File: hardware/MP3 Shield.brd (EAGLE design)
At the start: 53.3 x 59.7 mm, 52 parts, among them Q1 12.288MHz, U1 3.3V, U2 ARDUINO_SHIELD, U3 VS1053, U4 1.8V, U6 USD-SOCKET, U7 74HC4050 LVL CONVERTER

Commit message: More WIP.
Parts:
- removed U$7: LOGO-SFENEW, SparkFun:SFE-NEW-WEBLOGO
- removed U5: (no value), SparkFun:AUDIO-JACK-3.5MM-SMD
- added C17, C18: 10uF, SparkFun-Capacitors:EIA3216
- added C19, C20: 3.3nF, SparkFun-Capacitors:0603-CAP
- added J1: ISP/SPI, SparkFun:2X3
- added LOGO1: OSHW-LOGOS, SparkFun-Aesthetics:OSHW-LOGO-S
- added LOGO2: SFE_LOGO_NAME_FLAME.1_INCH, SparkFun-Aesthetics:SFE_LOGO_NAME_FLAME_.1
- added R15, R16: 10K, SparkFun-Resistors:0603-RES
- added R21, R22: 470, SparkFun-Resistors:0603-RES
- added R23: 1K, SparkFun-Resistors:0603-RES
- added SJ4: NC, SparkFun:SJ_2S-TRACE
- added SJ7, SJ8, SJ9: JUMPER-PAD-3-2OF3_NC_BY_TRACE, SparkFun-Passives:PAD-JUMPER-3-2OF3_NC_BY_TRACE_YES_SILK_FULL_BOX
- C1, C6: device SparkFun:EIA3216 -> SparkFun-Capacitors:EIA3216
- C10, C11, C12, C13, C14, C15, C16, C2, C3, C4, C5, C7, C8, C9: device SparkFun:0402-CAP -> SparkFun-Capacitors:0603-CAP
- JP1: value Line Output -> (none); device SparkFun:1X03 -> SparkFun-Connectors:AUDIO-JACK-3.5MM-SMD
- JP3: value External Speaker -> Optional
- LED1: device SparkFun:LED-0603 -> SparkFun-LED:LED-0603
- R1, R10, R11, R12, R13, R14, R2, R3, R4, R5, R6, R7, R8, R9: device SparkFun:0402-RES -> SparkFun-Resistors:0603-RES
- S2: device SparkFun:TACTILE_SWITCH_SMD -> SparkFun-Electromechanical:TACTILE_SWITCH_SMD
- U1: device SparkFun:SOT23-5 -> SparkFun-PowerIC:SOT23-5
- U2: value ARDUINO_SHIELD -> ARDUINO_R3_SHIELD; device SparkFun:DUEMILANOVE_SHIELD -> SparkFun-Boards:UNO_R3_SHIELD
- U3: device SparkFun:LQFP-48 -> SparkFun-DigitalIC:LQFP-48
- U4: device SparkFun:SC70 -> SparkFun-PowerIC:SC70
- U7: device SparkFun:SO016 -> SparkFun-DigitalIC:SO016
- moved JP1 73.8 mm to (27.9, 0.00), turned to 90 degrees
- moved C1 10.2 mm to (43.2, 35.6)
- moved LED1 10.2 mm to (43.2, 53.3), turned to 90 degrees
- moved R8 10.2 mm to (43.2, 52.1)
- moved C2 10.2 mm to (43.2, 38.1)
- moved U4 10.2 mm to (43.2, 40.6)
- moved C4 10.2 mm to (43.2, 50.8)
- moved C5 10.2 mm to (43.2, 45.7)
- moved C6 10.2 mm to (43.2, 43.2)
- moved TP1 10.2 mm to (40.6, 45.7)
- moved U1 10.2 mm to (43.2, 48.3)
- moved U$8 6.35 mm to (36.1, 46.1)
- moved S2 6.35 mm to (49.5, 12.7), turned to 90 degrees
- moved C12 1.80 mm to (38.1, 34.3)
- moved C10 1.80 mm to (38.1, 33.0)
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- renumbered SJ1 to SJ3
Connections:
- net N$1 renamed RCAP
- net N$73 renamed GPIO4
- new net /MUTE: R23.1
- new net 5V-MUTE: SJ4.2, U2.D5
- new net N$14: R23.2, SJ4.1
- new net N$17: C18.A, C20.1, R22.1
- new net N$19: C17.A, C19.1, R21.1
- new net SPKR-L: C17.C, R15.1
- new net SPKR-R: C18.C, R16.1
- net 3.3V: no longer R5.1
- net 5V-MOSI: now also J1.4
- net 5V-SCK: now also J1.3
- net GBUF: no longer JP3.1, U5.SLEEVE
- net GND: now also C19.2, C20.2, J1.6, R15.2, R16.2, R5.1, SJ9.1
- net LEFT: now also R21.2; no longer JP3.3, U5.TIP
- net MISO: now also J1.1
- net RIGHT: now also R22.2; no longer JP3.2, U5.RING
- net VCC: now also J1.2
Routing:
- net 5V-SCK: track 16.5 -> 95.7 mm
- net 5V-MUTE: track 0.00 -> 65.6 mm, vias 0 -> 4
- net 5V-MOSI: track 13.3 -> 65.5 mm
- net MISO: track 53.3 -> 102.7 mm
- net VCC: track 17.5 -> 59.1 mm
- net RIGHT: track 50.6 -> 14.5 mm
- net 3.3V: track 129.2 -> 161.7 mm, vias 6 -> 8
- net LEFT: track 50.1 -> 32.3 mm
- net ARST: track 5.34 -> 15.3 mm
- net 1.8V: track 47.6 -> 54.0 mm, vias 3 -> 4
- net SPKR-L: track 0.00 -> 6.16 mm
- net MP3-RST: track 39.9 -> 45.4 mm
- net N$19: track 0.00 -> 5.06 mm
- net N$17: track 0.00 -> 5.06 mm
- net GND: track 20.0 -> 24.4 mm, vias 14 -> 17
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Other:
- board text added: "GBUF"
- board text added: "GND"
- board text added: "MP3 Player"
- board text added: "MUTE"
- board text added: "SJ1"
- board text added: "SPI"
- board text added: "Shield"
- board text added: "v1.4"
- board text removed: "4-1-11"

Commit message: Yet more WIP
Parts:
- removed R23: 1K, SparkFun-Resistors:0603-RES
- removed SJ7, SJ8, SJ9: JUMPER-PAD-3-2OF3_NC_BY_TRACE, SparkFun-Passives:PAD-JUMPER-3-2OF3_NC_BY_TRACE_YES_SILK_FULL_BOX
- added SJ1: NC, SparkFun:SJ_2S-TRACE
- added SJ5: AC Coupling L, SparkFun-Passives:PAD-JUMPER-3-2OF3_NC_BY_TRACE_YES_SILK_FULL_BOX
- SJ3: value NC -> AC Coupling Gnd; device SparkFun:SJ_2S-TRACE -> SparkFun-Passives:PAD-JUMPER-3-2OF3_NC_BY_TRACE_YES_SILK_FULL_BOX
- SJ4: value NC -> AC Coupling R; device SparkFun:SJ_2S-TRACE -> SparkFun-Passives:PAD-JUMPER-3-2OF3_NC_BY_TRACE_YES_SILK_FULL_BOX
- moved SJ3 43.0 mm to (38.1, 8.89), turned to 90 degrees
- moved R15 16.5 mm to (41.9, 24.1), turned to 0 degrees
- moved C17 14.0 mm to (35.6, 26.7), turned to 180 degrees
- moved R16 13.1 mm to (41.9, 30.5), turned to 0 degrees
- moved SJ4 10.9 mm to (38.1, 19.1), turned to 90 degrees
- moved C19 8.89 mm to (38.1, 24.1)
- moved R21 8.89 mm to (34.3, 24.1)
- moved C18 7.18 mm to (41.9, 27.9), turned to 180 degrees
- moved C20 5.08 mm to (38.1, 30.5)
- moved R22 5.08 mm to (34.3, 30.5)
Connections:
- removed net /MUTE: R23.1
- removed net 5V-MUTE: SJ4.2, U2.D5
- new net N$12: JP1.SLEEVE, JP3.1, SJ3.2
- new net N$13: JP1.RING, JP3.2, SJ4.2
- net 5V-GPIO1: now also SJ1.2; no longer SJ3.2
- net GBUF: now also SJ3.3
- net GND: now also SJ3.1; no longer SJ9.1
- net LEFT: now also SJ5.3
- net N$14: now also JP1.TIP, JP3.3, SJ5.2; no longer R23.2, SJ4.1
- net N$4: now also SJ1.1; no longer SJ3.1
- net RIGHT: now also SJ4.3
- net SPKR-L: now also SJ5.1
- net SPKR-R: now also SJ4.1
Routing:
- net 5V-MUTE: track 65.6 -> 0.00 mm, vias 4 -> 0
- net GBUF: track 43.5 -> 9.57 mm, vias 2 -> 1
- net 3.3V: track 161.7 -> 129.0 mm, vias 8 -> 5
- net LEFT: track 32.3 -> 15.8 mm, vias 2 -> 1
- net RIGHT: track 14.5 -> 7.54 mm, vias 2 -> 1
- net SPKR-L: track 6.16 -> 0.00 mm
- net N$19: track 5.06 -> 0.00 mm
- net N$17: track 5.06 -> 0.00 mm
- net SPKR-R: track 3.60 -> 0.00 mm
- net N$14: track 2.68 -> 0.00 mm
- net /MUTE: track 1.32 -> 0.00 mm
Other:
- board text added: "SJ3"
- board text added: "SJ3, SJ4, SJ5 -> for headphone output <- for line output"
- board text added: "SJ4"
- board text added: "SJ5"
- board text removed: "GBUF"
- board text removed: "GND"
- board text removed: "SJ1"

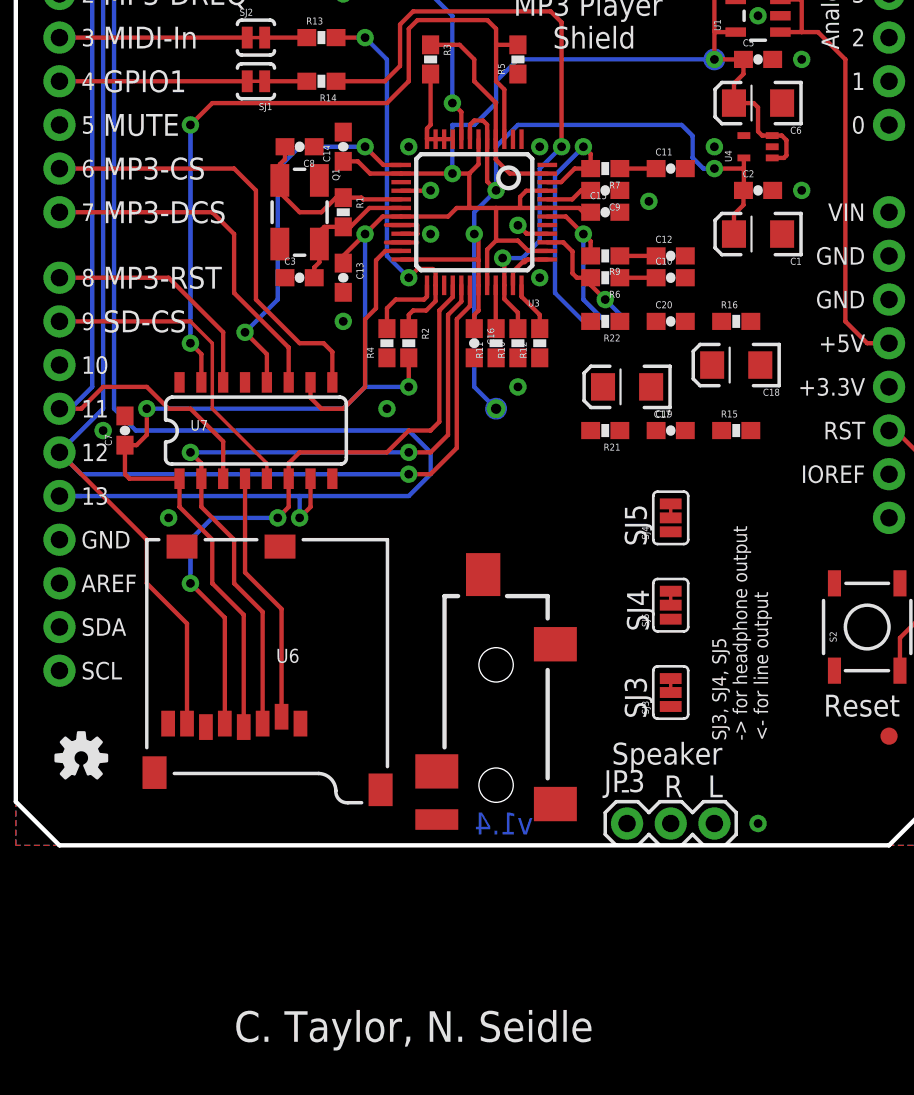
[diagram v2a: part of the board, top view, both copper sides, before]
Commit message: V1.5 ready for protos.
Board routed and ready for protos.
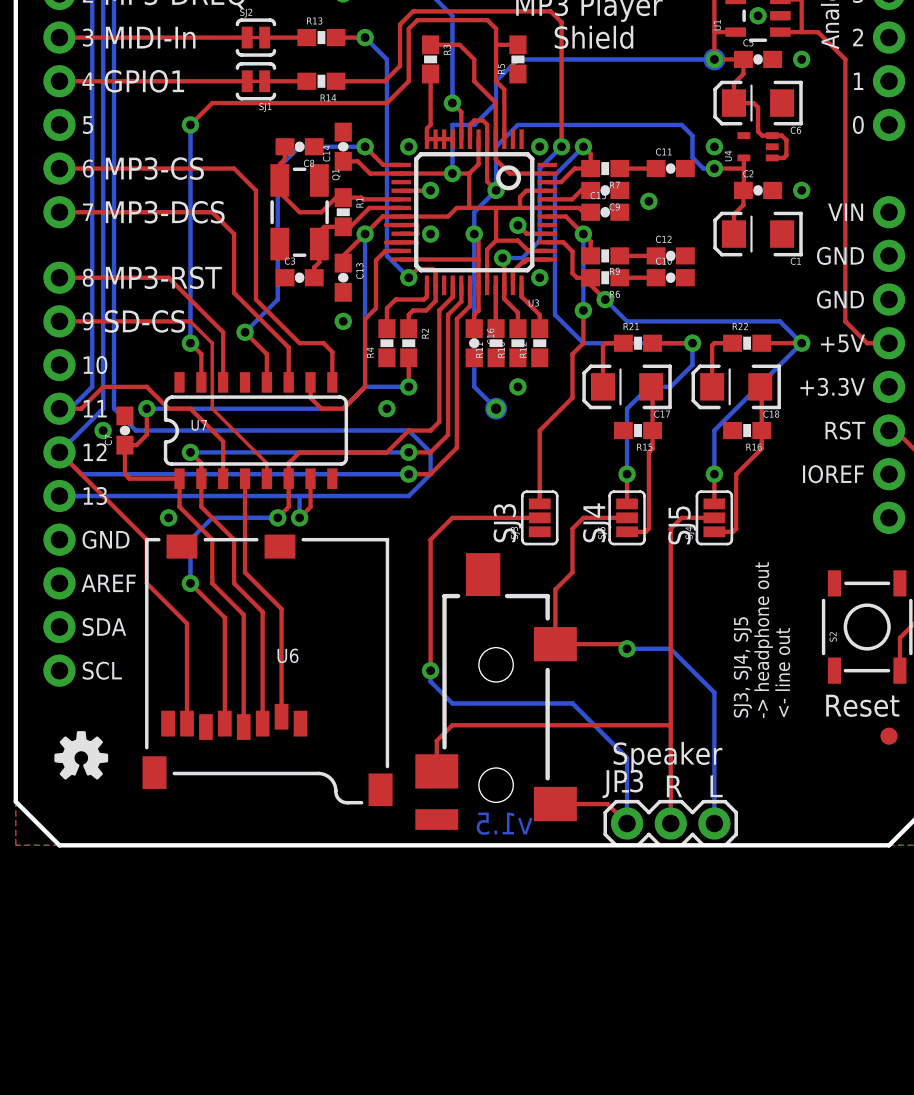
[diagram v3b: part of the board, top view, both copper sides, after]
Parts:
- removed C19, C20: 3.3nF, SparkFun-Capacitors:0603-CAP
- SJ3, SJ4, SJ5: device SparkFun-Passives:PAD-JUMPER-3-2OF3_NC_BY_TRACE_YES_SILK_FULL_BOX -> SparkFun-Passives:PAD-JUMPER-3-2OF3_NC_BY_PASTE_YES_SILK_FULL_BOX
- moved U$1 31.7 mm to (-7.62, -27.9)
- moved SJ3 12.7 mm to (30.5, 19.1)
- moved R22 8.35 mm to (42.5, 29.2), turned to 0 degrees
- moved R16 6.38 mm to (42.5, 24.1), turned to 180 degrees
- moved R15 5.71 mm to (36.2, 24.1), turned to 180 degrees
- moved SJ5 5.68 mm to (35.6, 19.1)
- moved R21 5.43 mm to (36.2, 29.2), turned to 0 degrees
- moved SJ4 2.54 mm to (40.6, 19.1)
- moved C18 1.27 mm to (41.9, 26.7)
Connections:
- net GND: no longer C19.2, C20.2
- net N$17: no longer C20.1
- net N$19: no longer C19.1
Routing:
- net N$12: track 0.00 -> 36.9 mm, vias 0 -> 1
- net N$13: track 0.00 -> 35.7 mm
- net N$14: track 0.00 -> 28.6 mm, vias 0 -> 1
- net RIGHT: track 7.54 -> 32.0 mm, vias 1 -> 3
- net LEFT: track 15.8 -> 37.4 mm, vias 1 -> 3
- net GBUF: track 9.57 -> 20.7 mm, vias 1 -> 2
- net SPKR-R: track 0.00 -> 10.2 mm
- net SPKR-L: track 0.00 -> 9.72 mm
- net N$19: track 0.00 -> 3.65 mm
- net N$17: track 0.00 -> 3.65 mm
- net GND: vias 17 -> 16
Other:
- board text added: "Byron Jacquot"
- board text added: "SJ3, SJ4, SJ5 -> headphone out <- line out"
- board text added: "v1.5"
- board text removed: "MUTE"
- board text removed: "SJ3, SJ4, SJ5 -> for headphone output <- for line output"
- board text removed: "v1.4"

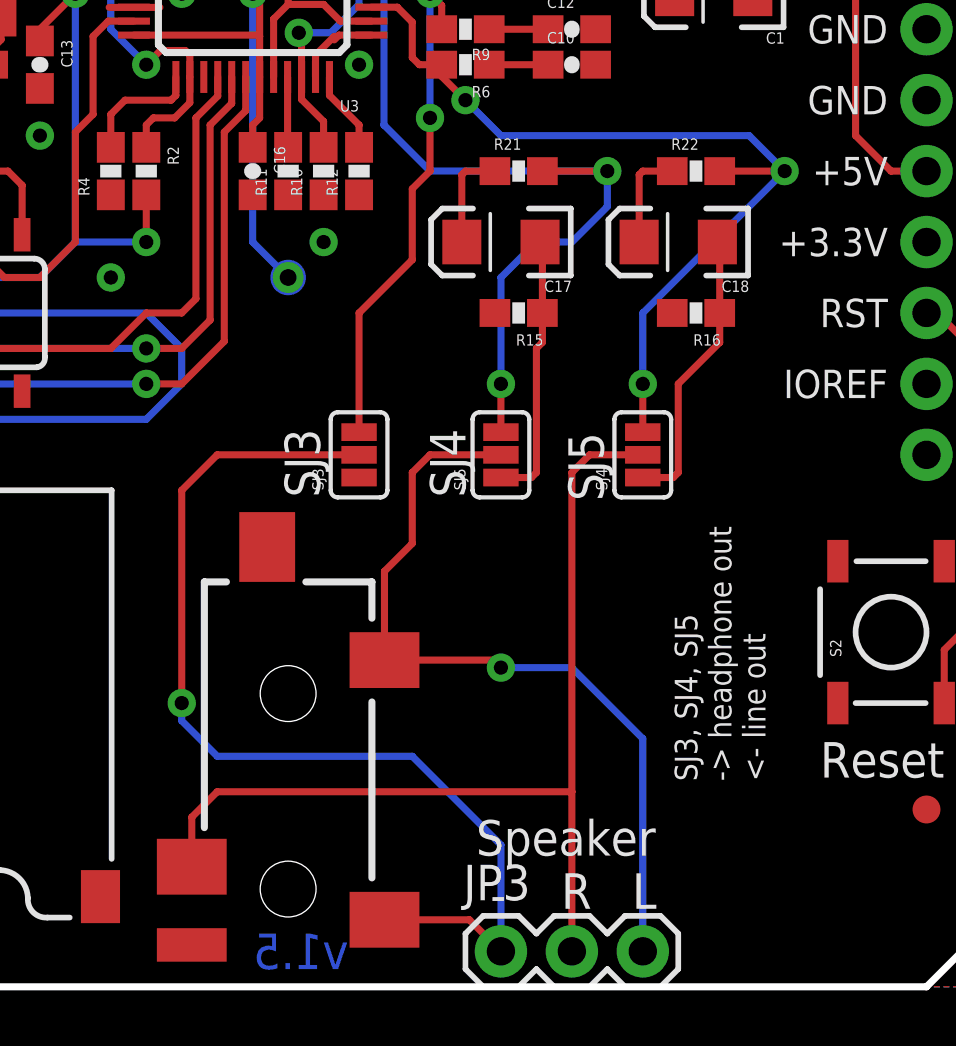
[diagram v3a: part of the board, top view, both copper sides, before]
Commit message: Ready to review for reds
Reorganized the solder jumpers for output coupling selection.
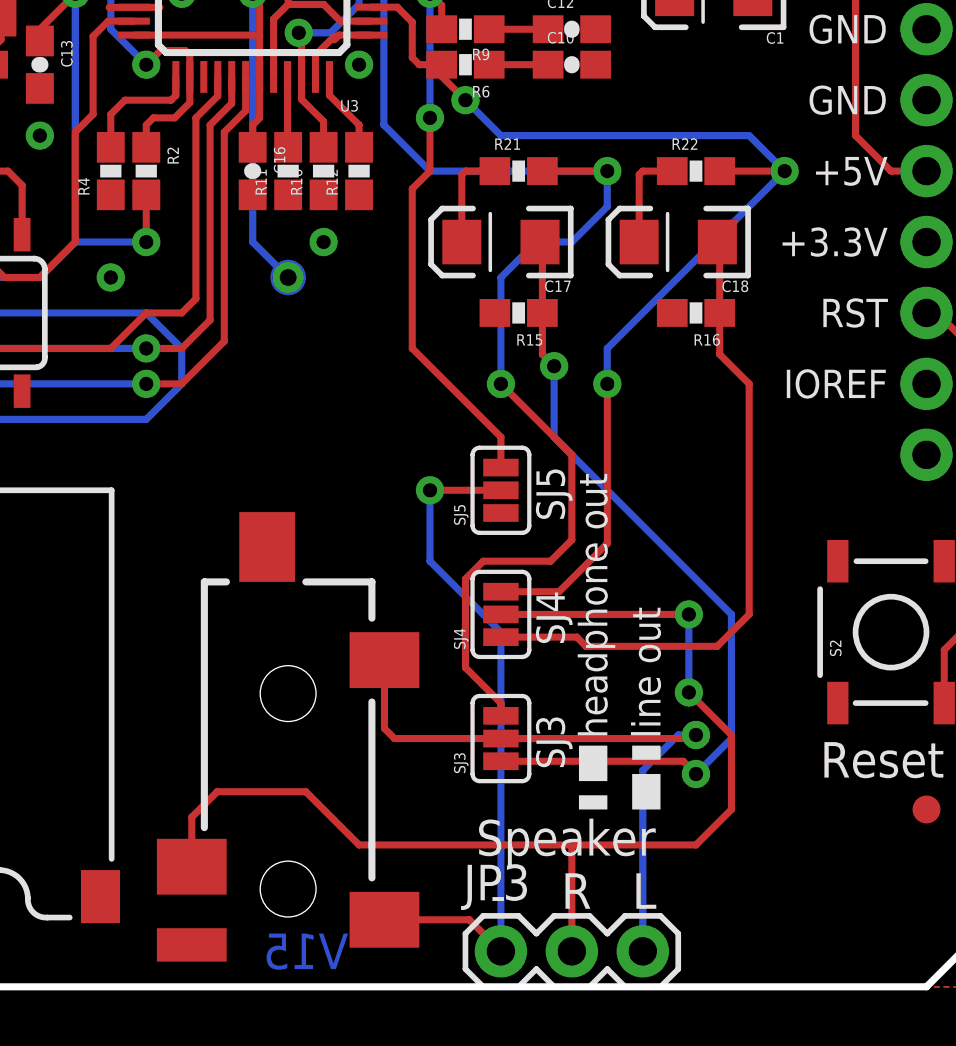
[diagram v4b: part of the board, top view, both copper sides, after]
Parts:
- SJ3: value AC Coupling Gnd -> AC Coupling L
- SJ5: value AC Coupling L -> AC Coupling Gnd
- moved SJ3 11.4 mm to (35.6, 8.89)
- moved SJ4 7.65 mm to (35.6, 13.3)
- moved SJ5 1.27 mm to (35.6, 17.8)
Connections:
- net GBUF: now also SJ5.3; no longer SJ3.3
- net GND: now also SJ5.1; no longer SJ3.1
- net LEFT: now also SJ3.3; no longer SJ5.3
- net N$12: now also SJ5.2; no longer SJ3.2
- net N$14: now also SJ3.2; no longer SJ5.2
- net SPKR-L: now also SJ3.1; no longer SJ5.1
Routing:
- net SPKR-L: track 9.72 -> 29.6 mm, vias 0 -> 2
- net LEFT: track 37.4 -> 52.2 mm
- net SPKR-R: track 10.2 -> 23.3 mm
- net N$12: track 36.9 -> 24.7 mm
- net RIGHT: track 32.0 -> 41.0 mm
- net N$14: track 28.6 -> 22.7 mm
- net N$13: track 35.7 -> 40.9 mm, vias 0 -> 2
- net GBUF: track 20.7 -> 22.5 mm
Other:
- board text added: "V15"
- board text added: "headphone out"
- board text added: "line out"
- board text removed: "SJ3, SJ4, SJ5 -> headphone out <- line out"
- board text removed: "v1.5"
